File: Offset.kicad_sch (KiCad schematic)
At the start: 18 parts, among them J1 Conn_01x02, J2 Conn_01x02, J3 Conn_01x02, U1 LM358

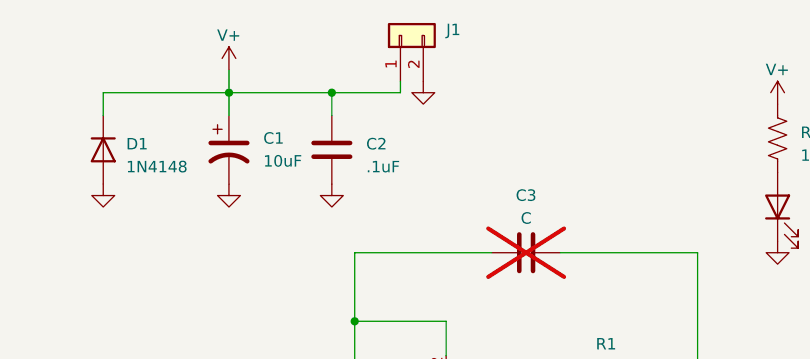
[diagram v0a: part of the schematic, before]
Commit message: Add PWR_FLAGs
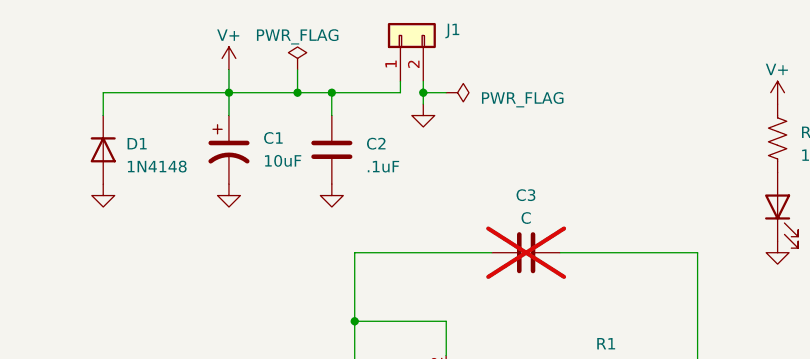
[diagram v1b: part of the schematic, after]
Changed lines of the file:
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@@
   (junction (at 142.24 88.9) (diameter 0) (color 0 0 0 0)
   )
+  (junction (at 135.89 50.8) (diameter 0) (color 0 0 0 0)
+  )
   (junction (at 128.27 50.8) (diameter 0) (color 0 0 0 0)
   )
@@
   )
   (junction (at 142.24 76.2) (diameter 0) (color 0 0 0 0)
+  )
+  (junction (at 149.86 50.8) (diameter 0) (color 0 0 0 0)
   )
   (junction (at 142.24 83.82) (diameter 0) (color 0 0 0 0)
@@
     (stroke (width 0) (type default))
   )
+  (wire (pts (xy 149.86 50.8) (xy 152.4 50.8))
+    (stroke (width 0) (type default))
+  )
   (wire (pts (xy 147.32 49.53) (xy 147.32 50.8))
     (stroke (width 0) (type default))
   )
+  (wire (pts (xy 135.89 48.26) (xy 135.89 50.8))
+    (stroke (width 0) (type default))
+  )
+  (wire (pts (xy 135.89 50.8) (xy 139.7 50.8))
+    (stroke (width 0) (type default))
+  )
+  (wire (pts (xy 149.86 50.8) (xy 149.86 49.53))
+    (stroke (width 0) (type default))
+  )
   (wire (pts (xy 125.73 107.95) (xy 137.16 107.95))
     (stroke (width 0) (type default))
@@
     (stroke (width 0) (type default))
   )
-  (wire (pts (xy 128.27 50.8) (xy 139.7 50.8))
+  (wire (pts (xy 128.27 50.8) (xy 135.89 50.8))
     (stroke (width 0) (type default))
   )
@@
     (stroke (width 0) (type default))
   )
+  (wire (pts (xy 149.86 52.07) (xy 149.86 50.8))
+    (stroke (width 0) (type default))
+  )
   (wire (pts (xy 96.52 107.95) (xy 110.49 107.95))
     (stroke (width 0) (type default))
@@
         (path "/b9c335b0-b204-4837-ad88-f803b4ac701f"
           (reference "#PWR04") (unit 1)
+        )
+      )
+    )
+  )
+  (symbol (lib_id "power:PWR_FLAG") (at 152.4 50.8 270) (unit 1)
+    (in_bom yes) (on_board yes) (dnp no) (fields_autoplaced)
+    (property "Reference" "#FLG01" (at 154.305 50.8 0)
+      (effects (font (size 1.27 1.27)) hide)
+    )
+    (property "Value" "PWR_FLAG" (at 156.21 51.435 90)
+      (effects (font (size 1.27 1.27)) (justify left))
+    )
+    (property "Footprint" "" (at 152.4 50.8 0)
+      (effects (font (size 1.27 1.27)) hide)
+    )
+    (property "Datasheet" "~" (at 152.4 50.8 0)
+      (effects (font (size 1.27 1.27)) hide)
+    )
+    (pin "1")
+    (instances
+      (project "Offset"
+        (path "/b9c335b0-b204-4837-ad88-f803b4ac701f"
+          (reference "#FLG01") (unit 1)
         )
       )
@@
     )
   )
-  (symbol (lib_id "power:GND") (at 149.86 49.53 0) (unit 1)
-    (in_bom yes) (on_board yes) (dnp no) (fields_autoplaced)
-    (property "Reference" "#PWR03" (at 149.86 55.88 0)
-      (effects (font (size 1.27 1.27)) hide)
-    )
-    (property "Value" "GND" (at 149.86 54.61 0)
-      (effects (font (size 1.27 1.27)) hide)
-    )
-    (property "Footprint" "" (at 149.86 49.53 0)
-      (effects (font (size 1.27 1.27)) hide)
-    )
-    (property "Datasheet" "" (at 149.86 49.53 0)
+  (symbol (lib_id "power:GND") (at 149.86 52.07 0) (unit 1)
+    (in_bom yes) (on_board yes) (dnp no) (fields_autoplaced)
+    (property "Reference" "#PWR03" (at 149.86 58.42 0)
+      (effects (font (size 1.27 1.27)) hide)
+    )
+    (property "Value" "GND" (at 149.86 57.15 0)
+      (effects (font (size 1.27 1.27)) hide)
+    )
+    (property "Footprint" "" (at 149.86 52.07 0)
+      (effects (font (size 1.27 1.27)) hide)
+    )
+    (property "Datasheet" "" (at 149.86 52.07 0)
       (effects (font (size 1.27 1.27)) hide)
     )
@@
         )
       )
+    )
+  )
+  (symbol (lib_id "power:PWR_FLAG") (at 135.89 48.26 0) (unit 1)
+    (in_bom yes) (on_board yes) (dnp no) (fields_autoplaced)
+    (property "Reference" "#FLG02" (at 135.89 46.355 0)
+      (effects (font (size 1.27 1.27)) hide)
+    )
+    (property "Value" "PWR_FLAG" (at 135.89 44.45 0)
+      (effects (font (size 1.27 1.27)))
+    )
+    (property "Footprint" "" (at 135.89 48.26 0)
+      (effects (font (size 1.27 1.27)) hide)
+    )
+    (property "Datasheet" "~" (at 135.89 48.26 0)
+      (effects (font (size 1.27 1.27)) hide)
+    )
+    (pin "1")
+    (instances
+      (project "Offset"
+        (path "/b9c335b0-b204-4837-ad88-f803b4ac701f"
+          (reference "#FLG02") (unit 1)
+        )
+      )

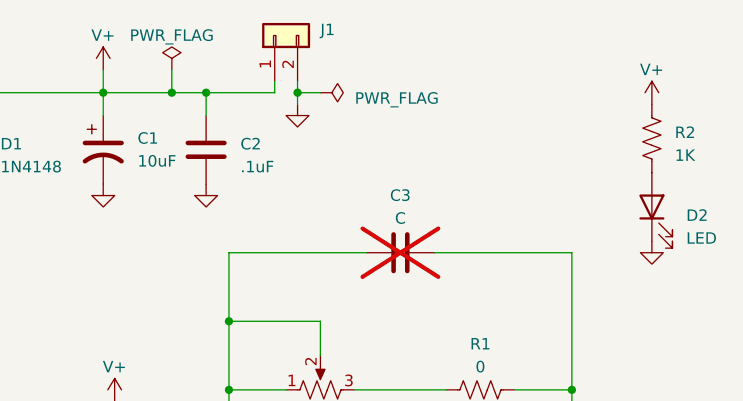
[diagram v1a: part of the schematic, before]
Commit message: Add simulation 0 reference
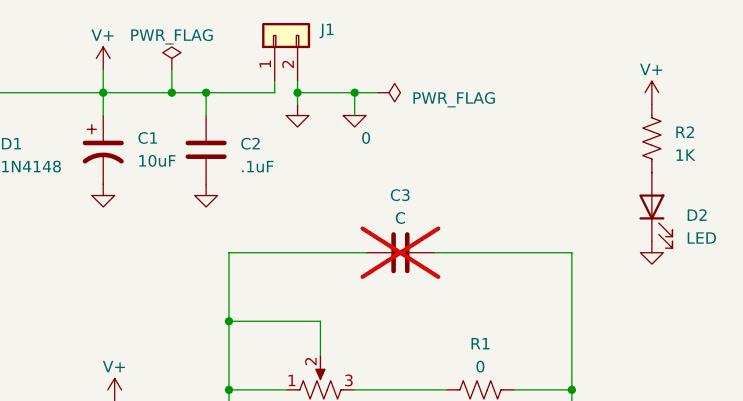
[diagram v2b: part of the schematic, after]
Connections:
- net GND renamed 0
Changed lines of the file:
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@@
   (junction (at 137.16 107.95) (diameter 0) (color 0 0 0 0)
+  )
+  (junction (at 156.21 50.8) (diameter 0) (color 0 0 0 0)
   )
   (junction (at 139.7 50.8) (diameter 0) (color 0 0 0 0)
@@
     (stroke (width 0) (type default))
   )
-  (wire (pts (xy 149.86 50.8) (xy 152.4 50.8))
+  (wire (pts (xy 149.86 50.8) (xy 156.21 50.8))
     (stroke (width 0) (type default))
   )
@@
     (stroke (width 0) (type default))
   )
+  (wire (pts (xy 156.21 50.8) (xy 158.75 50.8))
+    (stroke (width 0) (type default))
+  )
   (wire (pts (xy 180.34 83.82) (xy 180.34 105.41))
     (stroke (width 0) (type default))
@@
     (stroke (width 0) (type default))
   )
+  (wire (pts (xy 156.21 50.8) (xy 156.21 53.34))
+    (stroke (width 0) (type default))
+  )
   (wire (pts (xy 110.49 105.41) (xy 110.49 107.95))
     (stroke (width 0) (type default))
@@
     )
   )
-  (symbol (lib_id "power:PWR_FLAG") (at 152.4 50.8 270) (unit 1)
-    (in_bom yes) (on_board yes) (dnp no) (fields_autoplaced)
-    (property "Reference" "#FLG01" (at 154.305 50.8 0)
-      (effects (font (size 1.27 1.27)) hide)
-    )
-    (property "Value" "PWR_FLAG" (at 156.21 51.435 90)
-      (effects (font (size 1.27 1.27)) (justify left))
-    )
-    (property "Footprint" "" (at 152.4 50.8 0)
-      (effects (font (size 1.27 1.27)) hide)
-    )
-    (property "Datasheet" "~" (at 152.4 50.8 0)
+  (symbol (lib_id "power:PWR_FLAG") (at 158.75 50.8 270) (unit 1)
+    (in_bom yes) (on_board yes) (dnp no) (fields_autoplaced)
+    (property "Reference" "#FLG01" (at 160.655 50.8 0)
+      (effects (font (size 1.27 1.27)) hide)
+    )
+    (property "Value" "PWR_FLAG" (at 162.56 51.435 90)
+      (effects (font (size 1.27 1.27)) (justify left))
+    )
+    (property "Footprint" "" (at 158.75 50.8 0)
+      (effects (font (size 1.27 1.27)) hide)
+    )
+    (property "Datasheet" "~" (at 158.75 50.8 0)
       (effects (font (size 1.27 1.27)) hide)
     )
@@
         )
       )
+    )
+  )
+  (symbol (lib_id "Simulation_SPICE:0") (at 156.21 53.34 0) (unit 1)
+    (in_bom yes) (on_board yes) (dnp no)
+    (property "Reference" "#GND01" (at 156.21 55.88 0)
+      (effects (font (size 1.27 1.27)) hide)
+    )
+    (property "Value" "0" (at 157.48 55.88 0)
+      (effects (font (size 1.27 1.27)))
+    )
+    (property "Footprint" "" (at 156.21 53.34 0)
+      (effects (font (size 1.27 1.27)) hide)
+    )
+    (property "Datasheet" "~" (at 156.21 53.34 0)
+      (effects (font (size 1.27 1.27)) hide)
+    )
+    (pin "1")
+    (instances
+      (project "Offset"
+        (path "/b9c335b0-b204-4837-ad88-f803b4ac701f"
+          (reference "#GND01") (unit 1)
+        )
+      )
